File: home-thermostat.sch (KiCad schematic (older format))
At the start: 8 parts

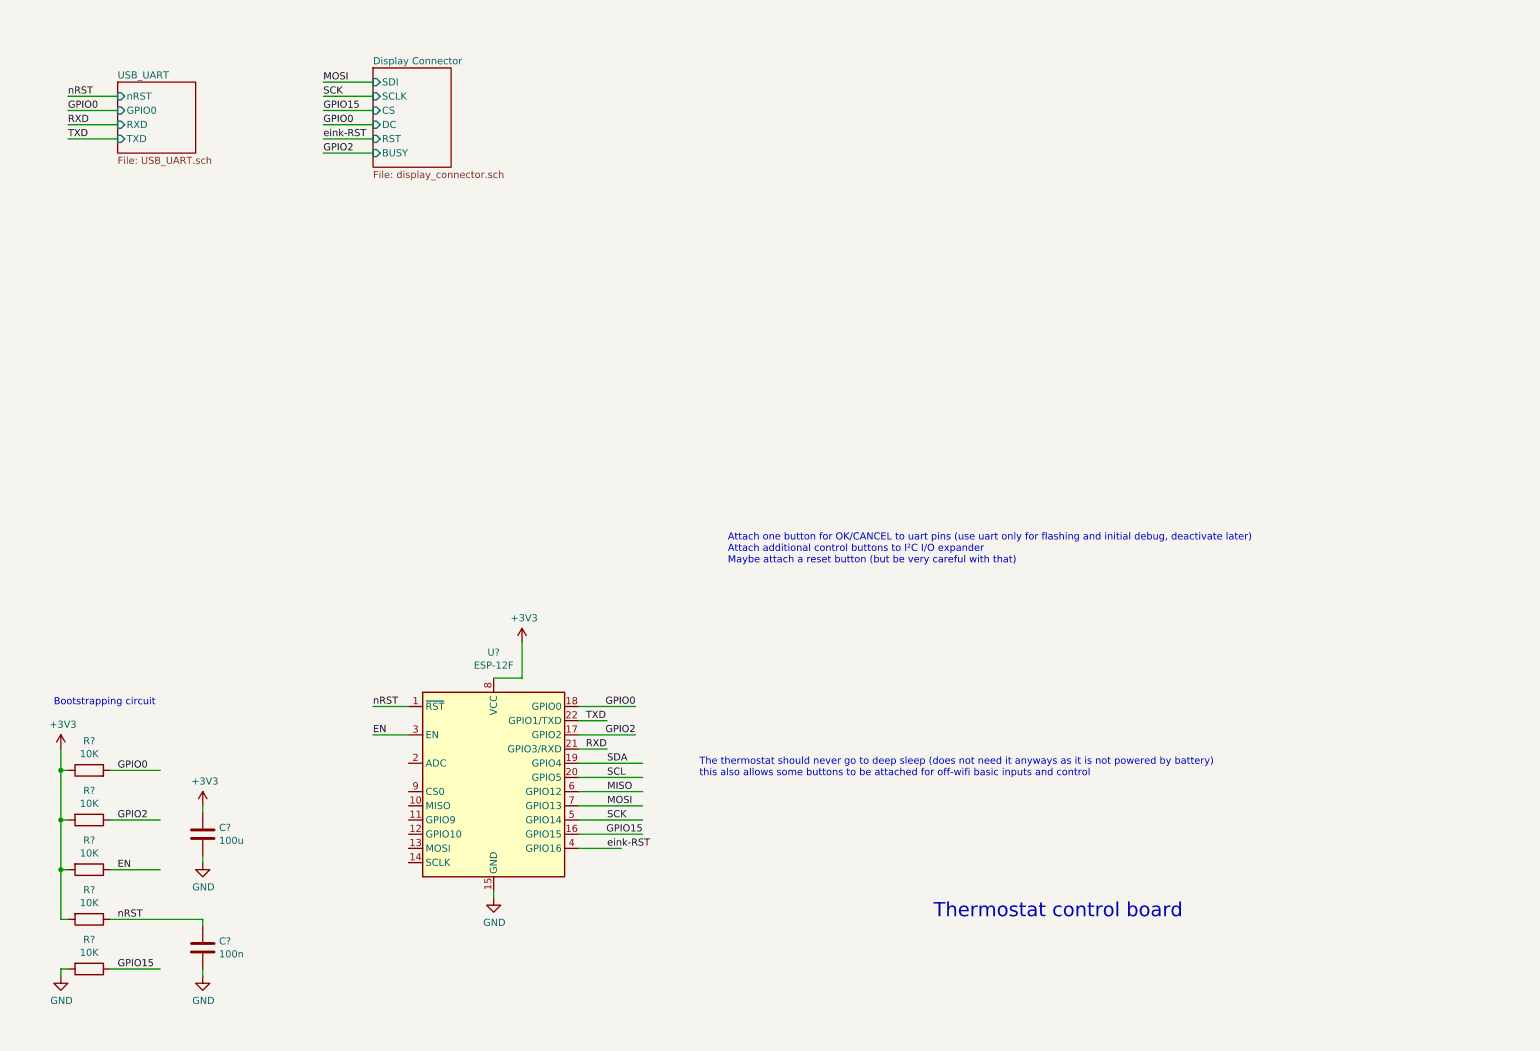
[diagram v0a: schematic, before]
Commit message: Added power supply and thermosthat control circuitry.
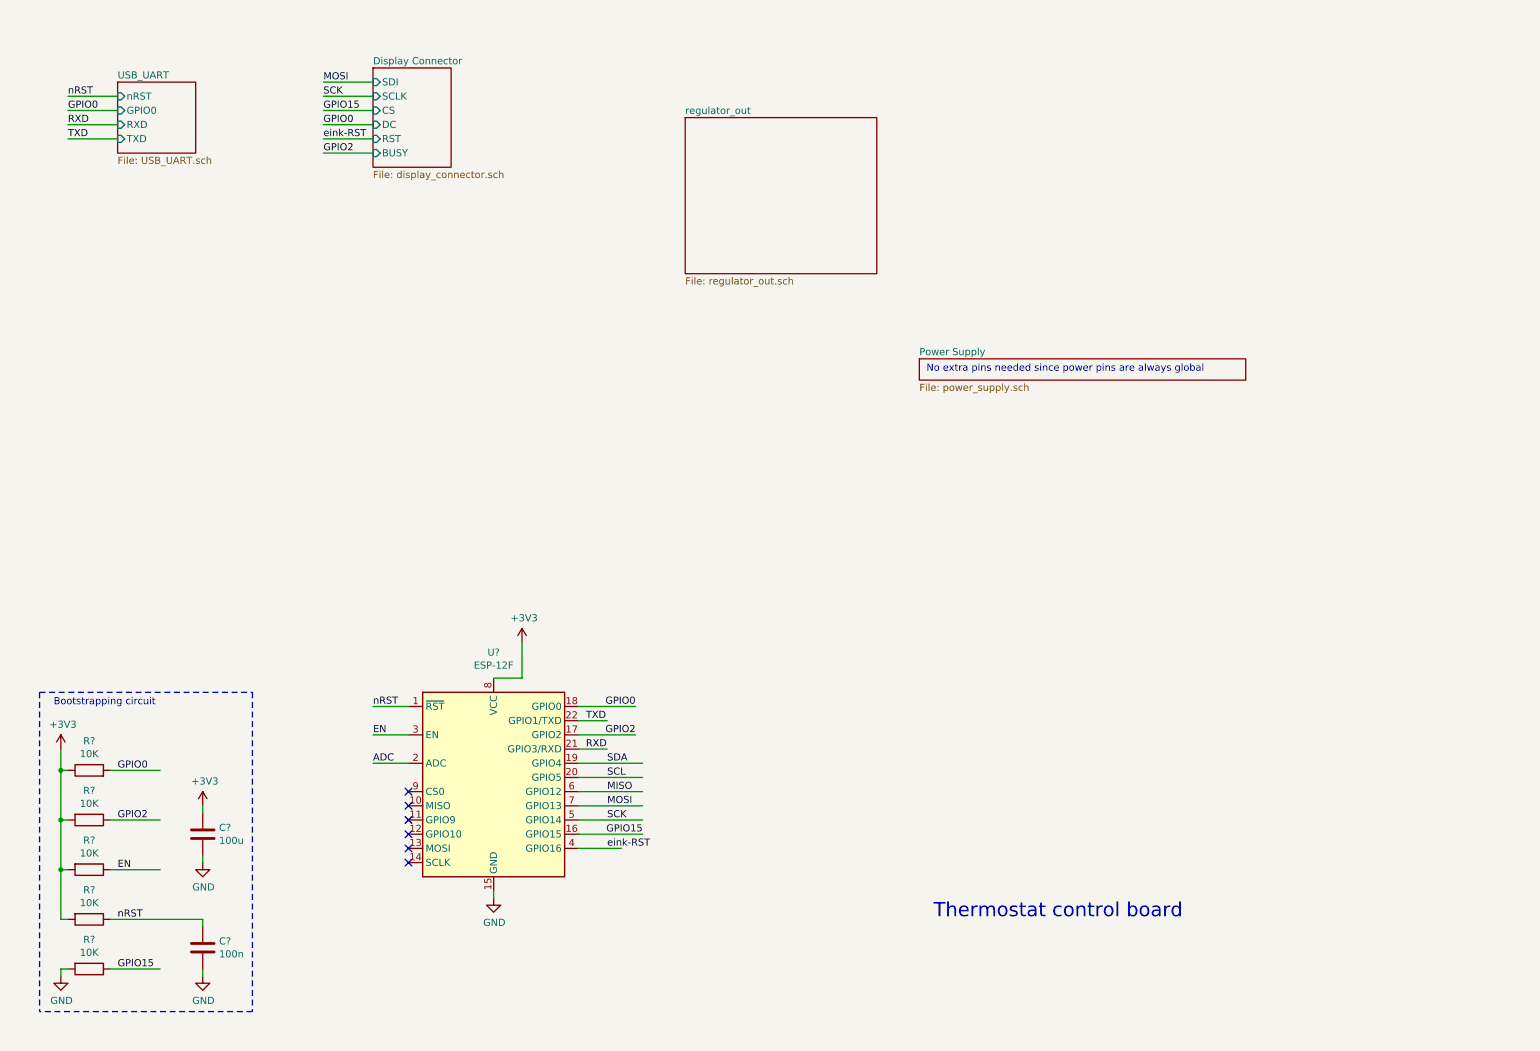
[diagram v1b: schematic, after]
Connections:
- net labels added: ADC
- wire segments 45 -> 46
- no-connect marks 0 -> 6
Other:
- note added: "No extra pins needed since power pins are always global"
- note removed: "Attach one button for OK/CANCEL to uart pins (use uart only for flashing and initial debug, deactivate later)\nAttach additional control buttons to I²C I/O expander\nMaybe attach a reset button (but be very careful with that)"
- note removed: "The thermostat should never go to deep sleep (does not need it anyways as it is not powered by battery)\nthis also allows some buttons to be attached for off-wifi basic inputs and control"
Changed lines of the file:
@@
 $Descr A4 11693 8268
 encoding utf-8
-Sheet 1 3
+Sheet 1 5
 Title ""
 Date ""
@@
 Text Label 2700 1400 0    50   ~ 0
 eink-RST
-Text Notes 5350 5900 0    50   ~ 0
-The thermostat should never go to deep sleep (does not need it anyways as it is not powered by battery)\nthis also allows some buttons to be attached for off-wifi basic inputs and control
-Text Notes 5550 4400 0    50   ~ 0
-Attach one button for OK/CANCEL to uart pins (use uart only for flashing and initial debug, deactivate later)\nAttach additional control buttons to I²C I/O expander\nMaybe attach a reset button (but be very careful with that)
+$Sheet
+S 5250 1250 1350 1100
+U 5E6A63AE
+F0 "regulator_out" 50
+F1 "regulator_out.sch" 50
+$EndSheet
+$Sheet
+S 6900 2950 2300 150
+U 5E8AC4D3
+F0 "Power Supply" 50
+F1 "power_supply.sch" 50
+$EndSheet
+Text Notes 6950 3050 0    50   ~ 0
+No extra pins needed since power pins are always global
+Wire Notes Line
+	700  5300 2200 5300
+Wire Notes Line
+	2200 5300 2200 7550
+Wire Notes Line
+	2200 7550 700  7550
+Wire Notes Line
+	700  5300 700  7550
+NoConn ~ 3300 6000
+NoConn ~ 3300 6100
+NoConn ~ 3300 6200
+NoConn ~ 3300 6300
+NoConn ~ 3300 6400
+NoConn ~ 3300 6500
+Text Label 3050 5800 0    50   ~ 0
+ADC
+Wire Wire Line
+	3050 5800 3300 5800
 $EndSCHEMATC

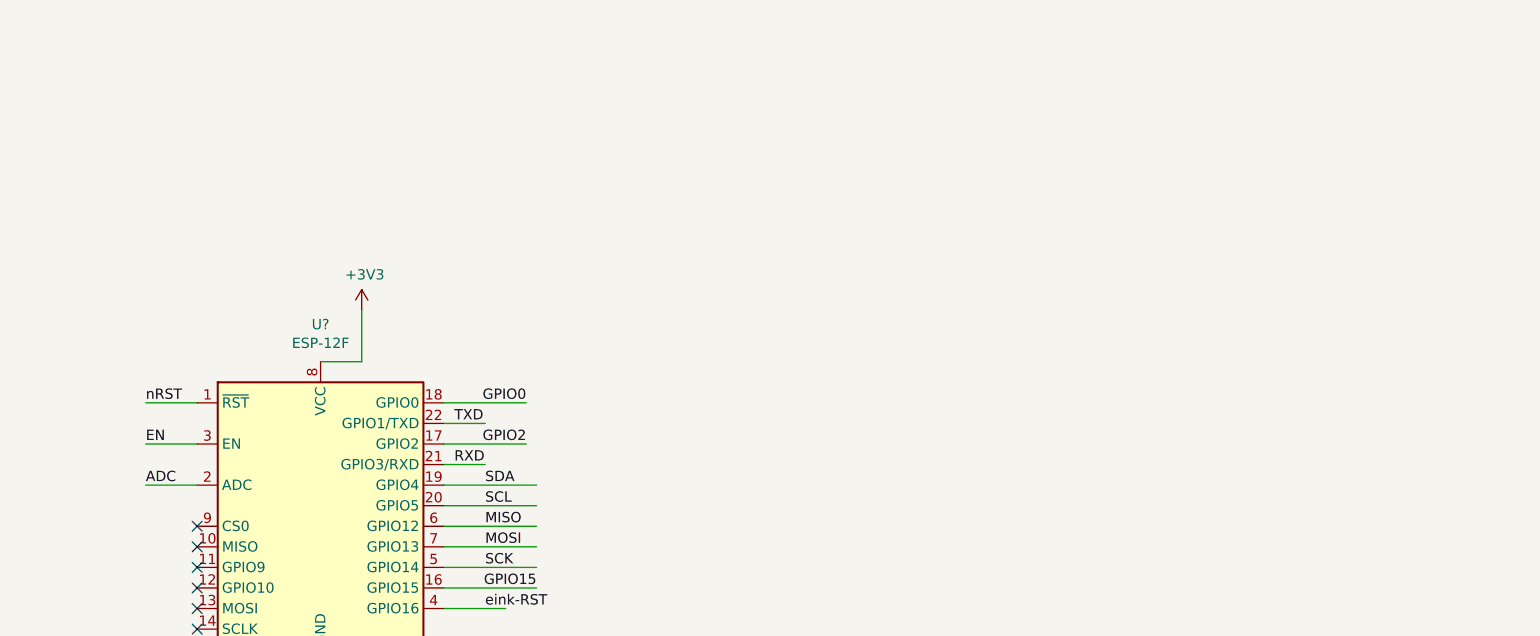
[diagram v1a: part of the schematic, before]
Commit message: Added RTC for timekeeping, AVR can now measure supply voltage.
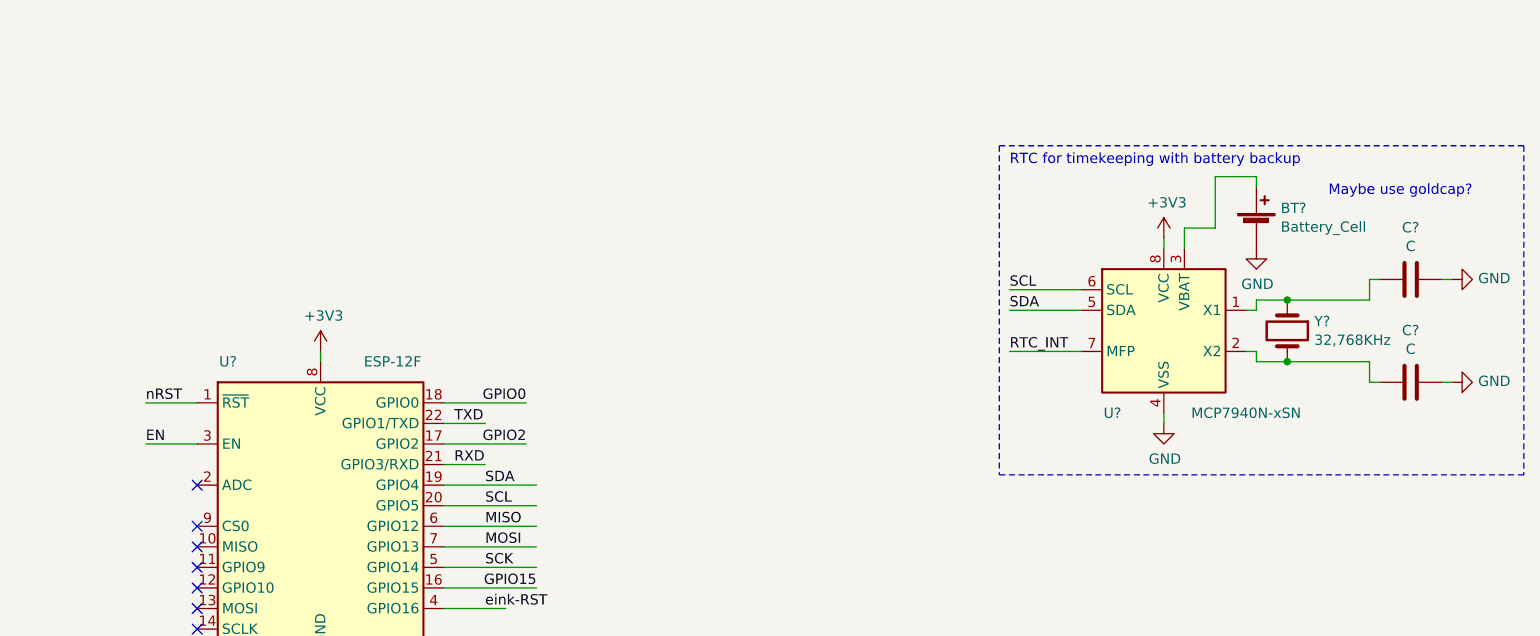
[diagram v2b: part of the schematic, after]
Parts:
- added BT?: Battery_Cell, symbol Device:Battery_Cell
- added C? (x2): C, symbol Device:C
- added U?: MCP7940N-xSN, symbol Timer:MCP7940N-xSN
- added Y?: 32,768KHz, symbol Device:Crystal
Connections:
- net labels added: RTC_INT
- net labels removed: ADC
- wire segments 46 -> 68
- no-connect marks 6 -> 7
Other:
- note added: "Maybe use goldcap?"
- note added: "RTC for timekeeping with battery backup"
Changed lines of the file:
@@
 U 1 1 5E5A73F8
 P 3900 6000
-F 0 "U?" H 3900 6981 50  0000 C CNN
-F 1 "ESP-12F" H 3900 6890 50  0000 C CNN
+F 0 "U?" H 3450 6800 50  0000 C CNN
+F 1 "ESP-12F" H 4250 6800 50  0000 C CNN
 F 2 "RF_Module:ESP-12E" H 3900 6000 50  0001 C CNN
 F 3 "http://wiki.ai-thinker.com/_media/esp8266/esp8266_series_modules_user_manual_v1.1.pdf" H 3550 6100 50  0001 C CNN
@@
 L power:+3V3 #PWR?
 U 1 1 5E5A88D5
-P 4100 4950
-F 0 "#PWR?" H 4100 4800 50  0001 C CNN
-F 1 "+3V3" H 4115 5123 50  0000 C CNN
-F 2 "" H 4100 4950 50  0001 C CNN
-F 3 "" H 4100 4950 50  0001 C CNN
-	1    4100 4950
-	1    0    0    -1
-$EndComp
-Wire Wire Line
-	3900 5200 4100 5200
-Wire Wire Line
-	4100 5200 4100 4950
+P 3900 5150
+F 0 "#PWR?" H 3900 5000 50  0001 C CNN
+F 1 "+3V3" H 3915 5323 50  0000 C CNN
+F 2 "" H 3900 5150 50  0001 C CNN
+F 3 "" H 3900 5150 50  0001 C CNN
+	1    3900 5150
+	1    0    0    -1
+$EndComp
 Wire Wire Line
 	3300 5400 3050 5400
@@
 NoConn ~ 3300 6400
 NoConn ~ 3300 6500
-Text Label 3050 5800 0    50   ~ 0
-ADC
-Wire Wire Line
-	3050 5800 3300 5800
+NoConn ~ 3300 5800
+$Comp
+L Timer:MCP7940N-xSN U?
+U 1 1 5E93A4D3
+P 8000 5050
+AR Path="/5E9313E4/5E93A4D3" Ref="U?"  Part="1"
+AR Path="/5E93A4D3" Ref="U?"  Part="1"
+F 0 "U?" H 7750 4650 50  0000 C CNN
+F 1 "MCP7940N-xSN" H 8400 4650 50  0000 C CNN
+F 2 "" H 8000 5050 50  0001 C CNN
+F 3 "http://ww1.microchip.com/downloads/en/DeviceDoc/20005010F.pdf" H 8000 5050 50  0001 C CNN
+	1    8000 5050
+	1    0    0    -1
+$EndComp
+Wire Wire Line
+	7250 4850 7600 4850
+$Comp
+L Device:Crystal Y?
+U 1 1 5E93A4DD
+P 8600 5050
+AR Path="/5E9313E4/5E93A4DD" Ref="Y?"  Part="1"
+AR Path="/5E93A4DD" Ref="Y?"  Part="1"
+F 0 "Y?" V 8554 5181 50  0000 L CNN
+F 1 "32,768KHz" V 8645 5181 50  0000 L CNN
+F 2 "" H 8600 5050 50  0001 C CNN
+F 3 "~" H 8600 5050 50  0001 C CNN
+	1    8600 5050
+	0    1    1    0
+$EndComp
+Wire Wire Line
+	8400 4950 8450 4950
+Wire Wire Line
+	8450 4950 8450 4900
+Wire Wire Line
+	8450 4900 8600 4900
+Connection ~ 8600 4900
+Wire Wire Line
+	8600 4900 9000 4900
+Wire Wire Line
+	8400 5150 8450 5150
+Wire Wire Line
+	8450 5150 8450 5200
+Wire Wire Line
+	8450 5200 8600 5200
+Connection ~ 8600 5200
+Wire Wire Line
+	8600 5200 9000 5200
+$Comp
+L Device:C C?
+U 1 1 5E93A4ED
+P 9200 5300
+AR Path="/5E9313E4/5E93A4ED" Ref="C?"  Part="1"
+AR Path="/5E93A4ED" Ref="C?"  Part="1"
+F 0 "C?" V 8948 5300 50  0000 C CNN
+F 1 "C" V 9039 5300 50  0000 C CNN
+F 2 "" H 9238 5150 50  0001 C CNN
+F 3 "~" H 9200 5300 50  0001 C CNN
+	1    9200 5300
+	0    1    1    0
+$EndComp
+$Comp
+L Device:C C?
+U 1 1 5E93A4F3
+P 9200 4800
+AR Path="/5E9313E4/5E93A4F3" Ref="C?"  Part="1"
+AR Path="/5E93A4F3" Ref="C?"  Part="1"
+F 0 "C?" V 8948 4800 50  0000 C CNN
+F 1 "C" V 9039 4800 50  0000 C CNN
+F 2 "" H 9238 4650 50  0001 C CNN
+F 3 "~" H 9200 4800 50  0001 C CNN
+	1    9200 4800
+	0    1    1    0
+$EndComp
+Wire Wire Line
+	9000 4900 9000 4800
+Wire Wire Line
+	9000 4800 9050 4800
+Wire Wire Line
+	9000 5200 9000 5300
+Wire Wire Line
+	9000 5300 9050 5300
+$Comp
+L power:GND #PWR?
+U 1 1 5E93A4FD
+P 9400 4800
+AR Path="/5E9313E4/5E93A4FD" Ref="#PWR?"  Part="1"
+AR Path="/5E93A4FD" Ref="#PWR?"  Part="1"
+F 0 "#PWR?" H 9400 4550 50  0001 C CNN
+F 1 "GND" V 9405 4672 50  0000 R CNN
+F 2 "" H 9400 4800 50  0001 C CNN
+F 3 "" H 9400 4800 50  0001 C CNN
+	1    9400 4800
+	0    -1   -1   0
+$EndComp
+Wire Wire Line
+	9400 4800 9350 4800
+$Comp
+L power:GND #PWR?
+U 1 1 5E93A504
+P 9400 5300
+AR Path="/5E9313E4/5E93A504" Ref="#PWR?"  Part="1"
+AR Path="/5E93A504" Ref="#PWR?"  Part="1"
+F 0 "#PWR?" H 9400 5050 50  0001 C CNN
+F 1 "GND" V 9405 5172 50  0000 R CNN
+F 2 "" H 9400 5300 50  0001 C CNN
+F 3 "" H 9400 5300 50  0001 C CNN
+	1    9400 5300
+	0    -1   -1   0
+$EndComp
+Wire Wire Line
+	9400 5300 9350 5300
+$Comp
+L power:GND #PWR?
+U 1 1 5E93A50B
+P 8000 5500
+AR Path="/5E9313E4/5E93A50B" Ref="#PWR?"  Part="1"
+AR Path="/5E93A50B" Ref="#PWR?"  Part="1"
+F 0 "#PWR?" H 8000 5250 50  0001 C CNN
+F 1 "GND" H 8005 5327 50  0000 C CNN
+F 2 "" H 8000 5500 50  0001 C CNN
+F 3 "" H 8000 5500 50  0001 C CNN
+	1    8000 5500
+	1    0    0    -1
+$EndComp
+Wire Wire Line
+	8000 5500 8000 5450
+$Comp
+L power:+3V3 #PWR?
+U 1 1 5E93A512
+P 8000 4600
+AR Path="/5E9313E4/5E93A512" Ref="#PWR?"  Part="1"
+AR Path="/5E93A512" Ref="#PWR?"  Part="1"
+F 0 "#PWR?" H 8000 4450 50  0001 C CNN
+F 1 "+3V3" H 8015 4773 50  0000 C CNN
+F 2 "" H 8000 4600 50  0001 C CNN
+F 3 "" H 8000 4600 50  0001 C CNN
+	1    8000 4600
+	1    0    0    -1
+$EndComp
+Wire Wire Line
+	8000 4600 8000 4650
+$Comp
+L Device:Battery_Cell BT?
+U 1 1 5E93A51B
+P 8450 4550
+AR Path="/5E9313E4/5E93A51B" Ref="BT?"  Part="1"
+AR Path="/5E93A51B" Ref="BT?"  Part="1"
+F 0 "BT?" H 8568 4646 50  0000 L CNN
+F 1 "Battery_Cell" H 8568 4555 50  0000 L CNN
+F 2 "" V 8450 4610 50  0001 C CNN
+F 3 "~" V 8450 4610 50  0001 C CNN
+	1    8450 4550
+	1    0    0    -1
+$EndComp
+Wire Wire Line
+	8100 4650 8100 4550
+Wire Wire Line
+	8100 4550 8250 4550
+Wire Wire Line
+	8250 4550 8250 4300
+Wire Wire Line
+	8250 4300 8450 4300
+Wire Wire Line
+	8450 4300 8450 4350
+$Comp
+L power:GND #PWR?
+U 1 1 5E93A526
+P 8450 4650
+AR Path="/5E9313E4/5E93A526" Ref="#PWR?"  Part="1"
+AR Path="/5E93A526" Ref="#PWR?"  Part="1"
+F 0 "#PWR?" H 8450 4400 50  0001 C CNN
+F 1 "GND" H 8455 4477 50  0000 C CNN
+F 2 "" H 8450 4650 50  0001 C CNN
+F 3 "" H 8450 4650 50  0001 C CNN
+	1    8450 4650
+	1    0    0    -1
+$EndComp
+Text Label 7250 4850 0    50   ~ 0
+SCL
+Text Label 7250 4950 0    50   ~ 0
+SDA
+Text Label 7250 5150 0    50   ~ 0
+RTC_INT
+Wire Wire Line
+	7250 5150 7600 5150
+Wire Wire Line
+	7250 4950 7600 4950
+Text Notes 7250 4250 0    50   ~ 0
+RTC for timekeeping with battery backup
+Wire Notes Line
+	7200 4150 9750 4150
+Wire Notes Line
+	9750 4150 9750 5750
+Wire Notes Line
+	9750 5750 7200 5750
+Wire Notes Line
+	7200 4150 7200 5750
+Wire Wire Line
+	3900 5150 3900 5200
+Text Notes 8800 4400 0    50   ~ 0
+Maybe use goldcap?
 $EndSCHEMATC
